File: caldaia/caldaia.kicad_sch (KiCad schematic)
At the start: 9 parts, among them U1 ESP32-DEVKITC, U2 DS18B20, U3 DS18B20, U4 DS18B20, U5 DS18B20, U6 DS18B20

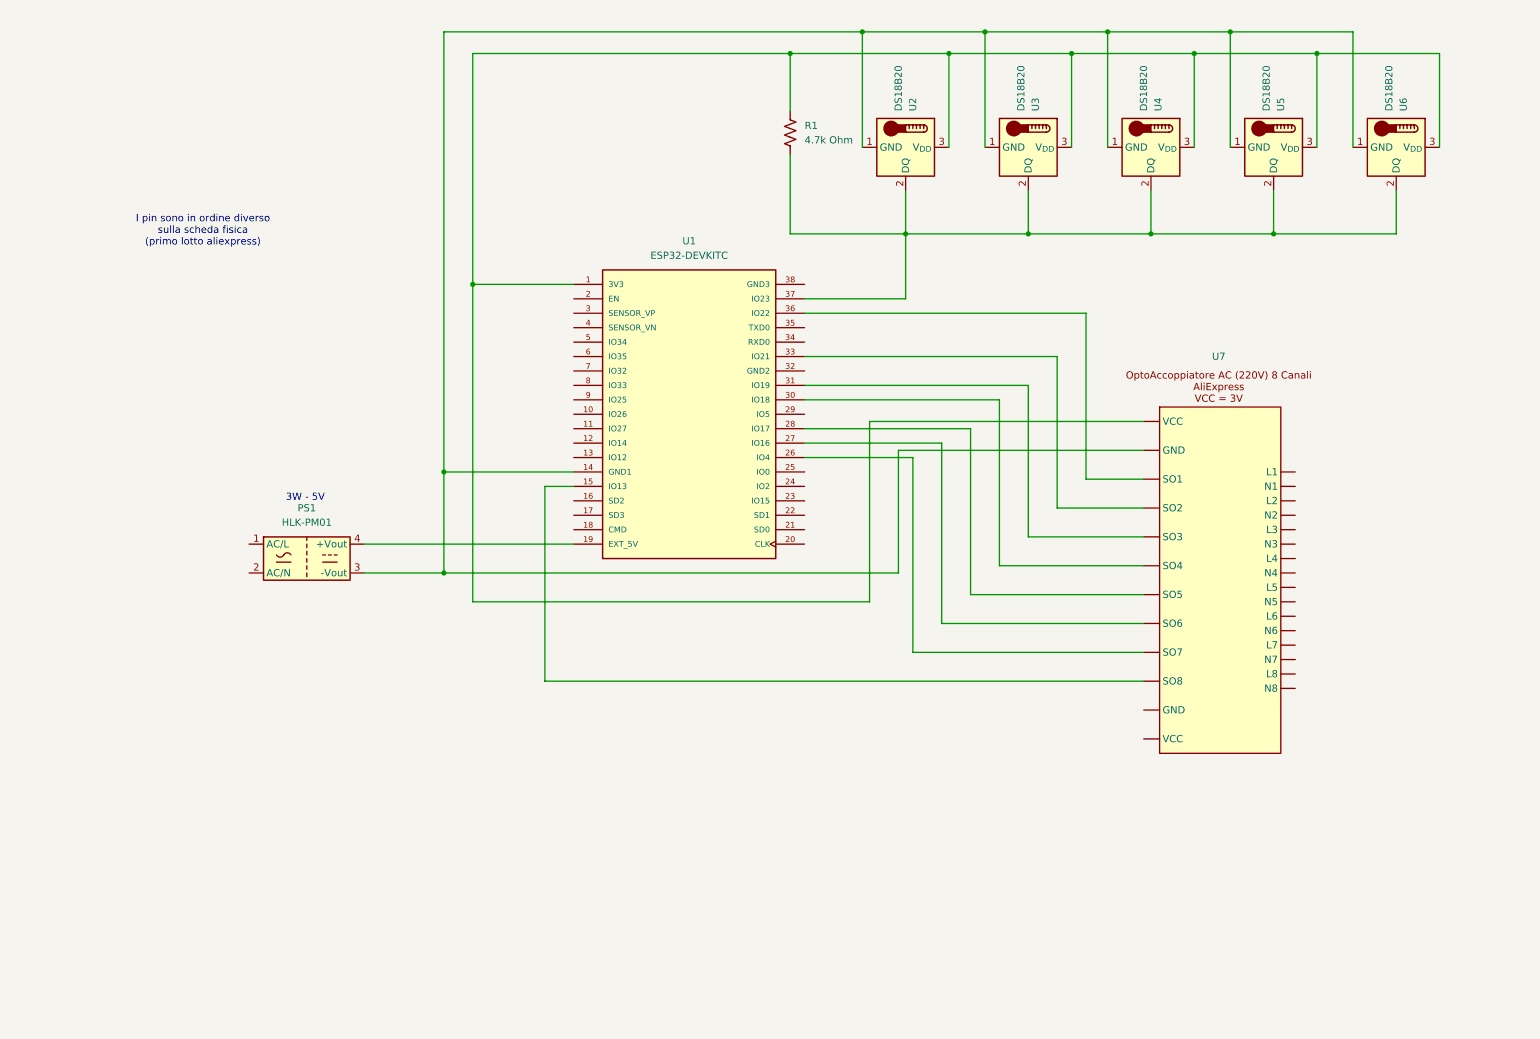
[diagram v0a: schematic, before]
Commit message: aggiornamenti caldaia, fusibile e morsetti
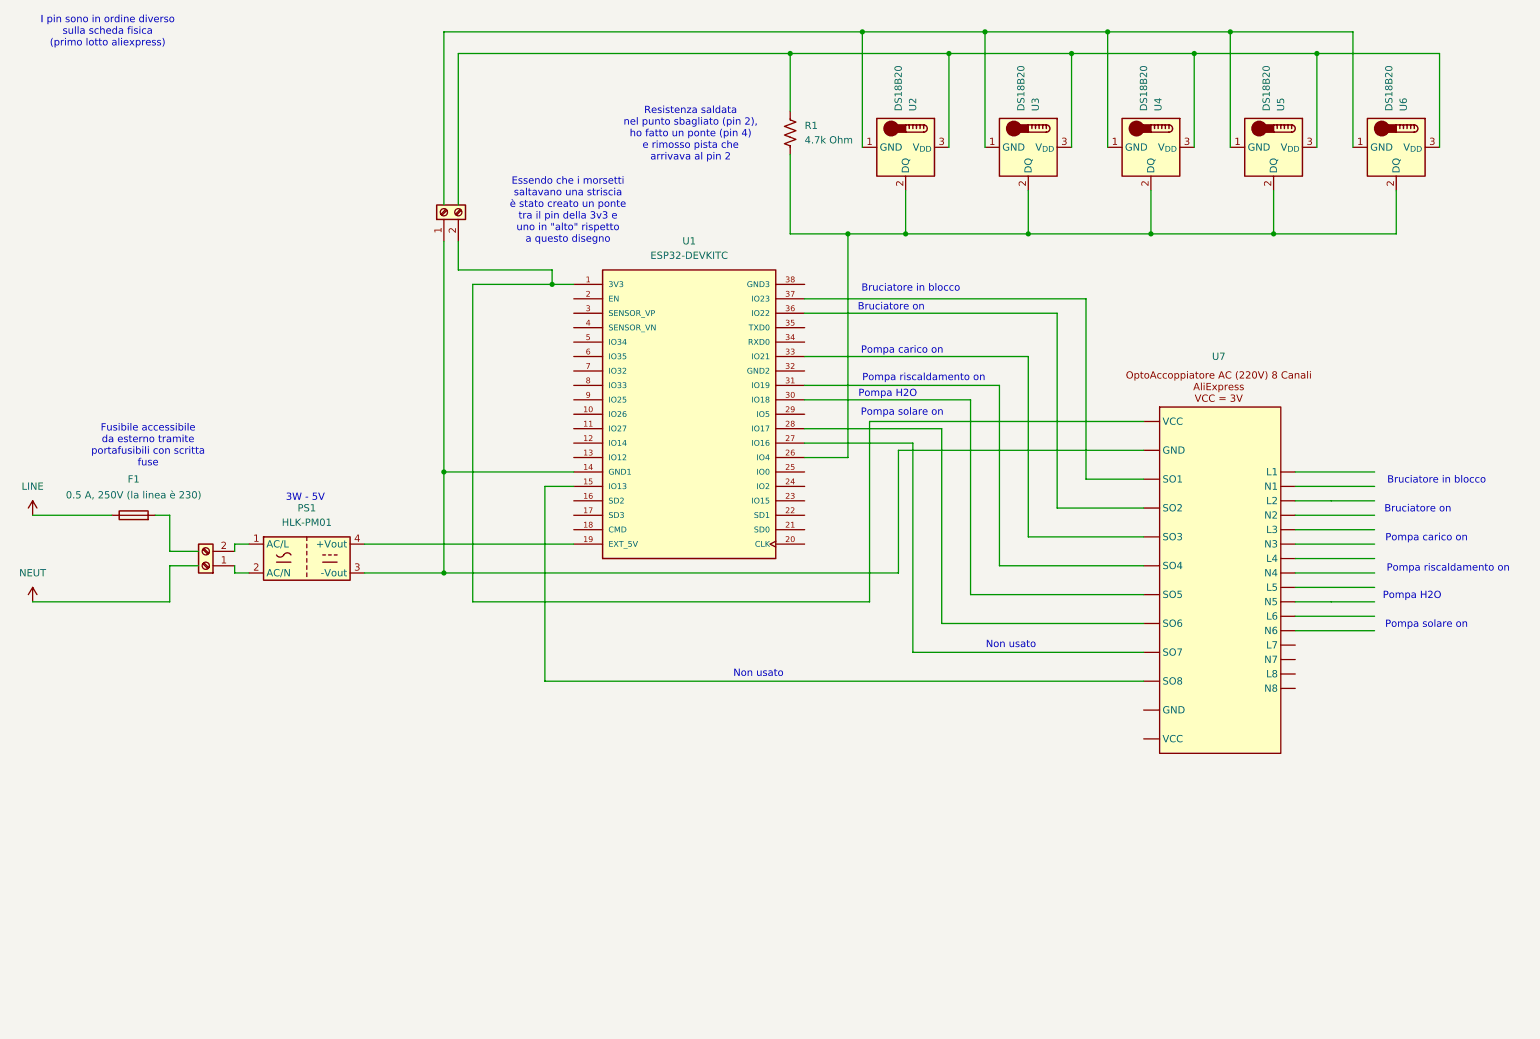
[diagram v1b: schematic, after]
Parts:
- added F1: 0.5 A, 250V (la linea è 230), symbol Device:Fuse
- added J1, J2: Screw_Terminal_01x02, symbol Connector:Screw_Terminal_01x02
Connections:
- net at U2.1 (GND), U3.1 (GND), U4.1 (GND)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: no longer PS1.3 (-Vout), U1.14 (GND1), U7. (N8)
- net at R1.2, U2.2 (DQ), U3.2 (DQ)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: now also U1.26 (IO4); no longer U1.37 (IO23)
- net at R1.1, U2.3 (V_{DD}), U3.3 (V_{DD})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: no longer U1.1 (3V3), U7. (N8)
- net at U7. (N8): now also U1.37 (IO23)
- net at PS1.1 (AC/L): now also J2.2 (Pin_2)
- net at PS1.2 (AC/N): now also J2.1 (Pin_1)
- new net: J1.1 (Pin_1), PS1.3 (-Vout), U1.14 (GND1), U7. (N8)
- new net: J1.2 (Pin_2), U1.1 (3V3), U7. (N8)
- new net LINE: F1.1
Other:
- note added: "Bruciatore in blocco"
- note added: "Bruciatore on"
- note added: "Essendo che i morsetti saltavano una striscia è stato creato un ponte tra il pin della 3v3 e uno in "alto" rispetto a questo disegno"
- note added: "Fusibile accessibile da esterno tramite portafusibili con scritta fuse"
- note added: "Non usato"
- note added: "Pompa H2O"
- note added: "Pompa carico on"
- note added: "Pompa riscaldamento on"
- note added: "Pompa solare on"
- note added: "Resistenza saldata nel punto sbagliato (pin 2), ho fatto un ponte (pin 4) e rimosso pista che arrivava al pin 2"

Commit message: Aggiunta descrizione in cartiglio
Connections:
- net at U7. (N8): now also U1.37 (IO23)
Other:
- note added: "28/12/2025"
- note added: "Sonde e Sensori Caldaia"
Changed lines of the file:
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@@
+		)
+	)
+	(text "Sonde e Sensori Caldaia"
+		(exclude_from_sim no)
+		(at 199.39 189.738 0)
+		(effects
+			(font
+				(size 1.27 1.27)
+			)
 		)
 	)
@@
 		(effects
 			(font
+				(size 1.27 1.27)
+			)
+		)
+	)
+	(text "28/12/2025"
+		(exclude_from_sim no)
+		(at 213.36 193.294 0)
+		(effects
+			(font
